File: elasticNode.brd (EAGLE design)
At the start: 82.2 x 52.5 mm, 106 parts, among them J1 ISP_CONN_6PIN, J2 FEMALE_HEADER_2X2, J3 FEMALE_HEADER_2X1, J4 FEMALE_HEADER_2X1, J5 FEMALE_HEADER_5X2, J6 FEMALE_HEADER_5X2, J7 JTAG_CONN_6PINTHT, J8 USB_CONNSMT, J9 USB_CONNSMT, U1 ATMEGA64AQFN, U10 LTC3419DFN, U11 ATMEGA32U4, U2 SST26VF032B, U3 MRF24J40MA, U4 SPARTAN6-LX9, U5 SST26VF032B, U6 PAC1720, U7 PAC1720, U8 PAC1720, U9 FT232RSSOP28, X1 12MHz, X2 50MHz, X3 32MHz

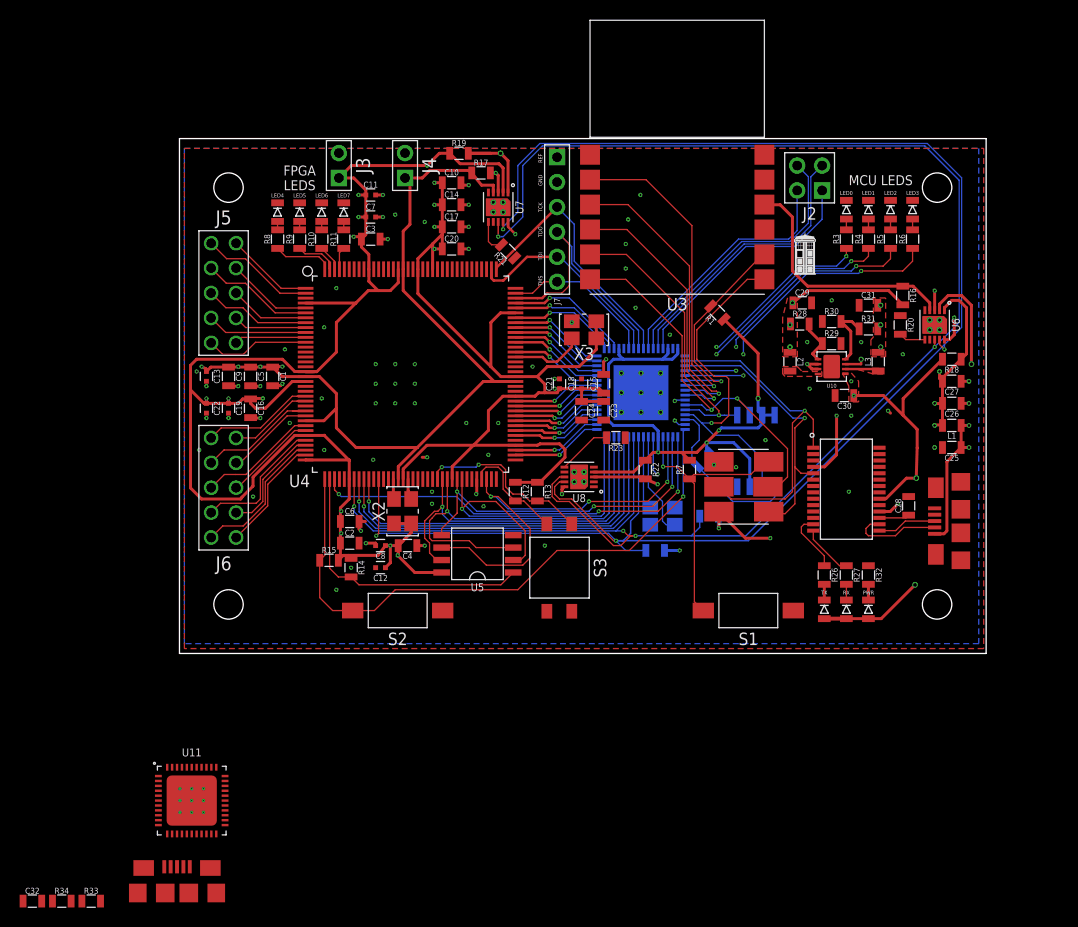
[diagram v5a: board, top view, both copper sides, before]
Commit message: first part of new layout
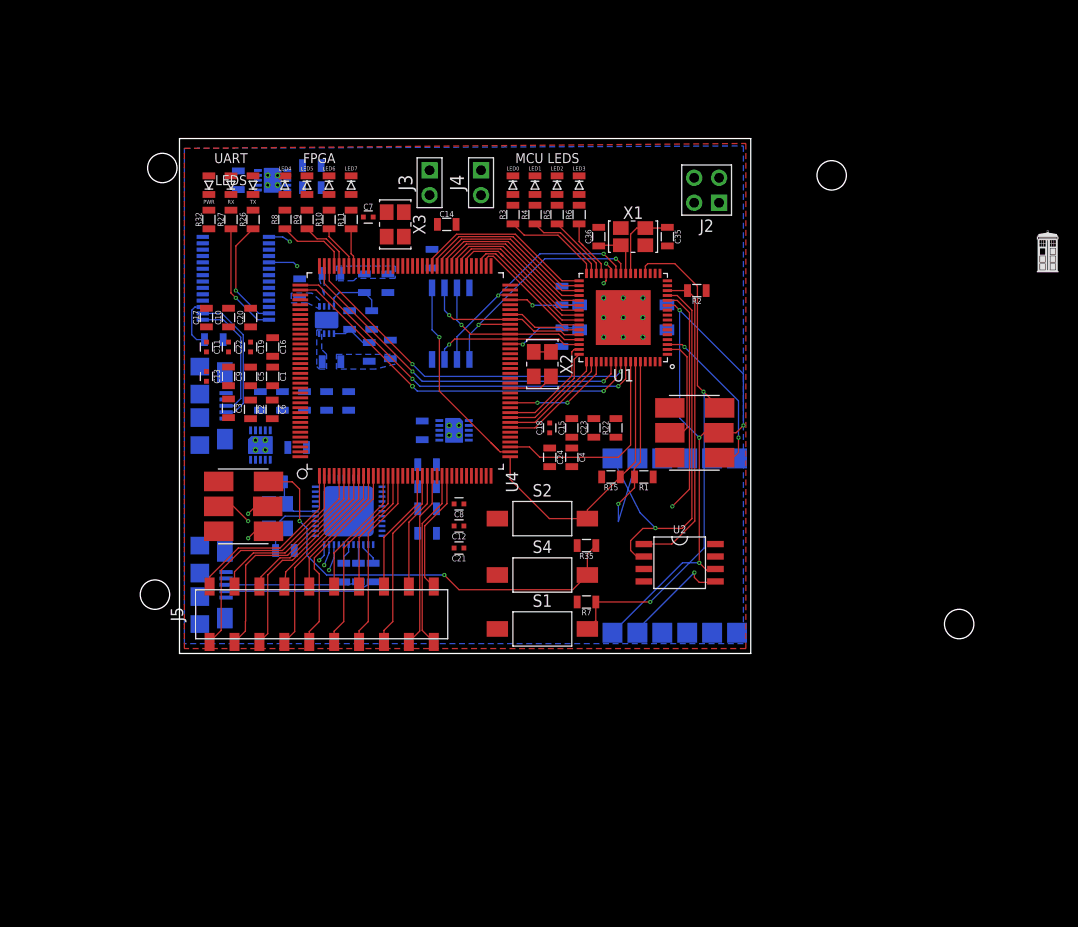
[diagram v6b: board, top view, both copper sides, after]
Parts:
- removed J6: FEMALE_HEADER_5X2, connectors:5X2_HEADER
- removed J7: JTAG_CONN_6PINTHT, connectors:6X1_HEADER
- added C33, C34: (no value), passive:0805
- added C35, C36: 20p, passive:0805
- added J10: ISP_CONN_6PIN, connectors:3X2_HEADER_SMT
- added R35: 15k, passive:0805
- added R36: .8, passive:0805
- added S4: SPST_BUTTON2PIN_SMT, connectors:SPST_2PIN_SMT
- added X4: 12MHz, passive:3.2X2.5_OSC
- J5: value FEMALE_HEADER_5X2 -> FEMALE_HEADER_10X2; device connectors:5X2_HEADER -> connectors:10X2_HEADER_SMT
- moved PWR 80.0 mm to (3.00, 47.8), turned to 270 degrees
- moved R32 76.4 mm to (3.00, 44.2), turned to 90 degrees
- moved RX 76.2 mm to (5.25, 47.8), turned to 270 degrees
- moved J8 73.2 mm to (4.75, 25.2), flipped to the bottom
- moved C28 72.8 mm to (3.50, 32.0), flipped to the bottom, turned to 180 degrees
- moved TX 72.6 mm to (7.50, 47.8), turned to 270 degrees
- moved R27 72.5 mm to (5.25, 44.2), turned to 90 degrees
- moved C25 70.7 mm to (8.25, 25.8), flipped to the bottom, turned to 90 degrees
- moved U6 69.8 mm to (8.25, 21.2), flipped to the bottom
- moved R26 68.6 mm to (7.50, 44.2), turned to 90 degrees
- moved L1 68.3 mm to (10.5, 25.8), flipped to the bottom, turned to 90 degrees
- moved C26 66.0 mm to (12.8, 25.8), flipped to the bottom, turned to 90 degrees
- moved U9 65.9 mm to (5.75, 38.2), flipped to the bottom, turned to 0 degrees
- moved C27 63.8 mm to (15.0, 25.8), flipped to the bottom, turned to 90 degrees
- moved R20 62.8 mm to (12.0, 21.0), flipped to the bottom, turned to 0 degrees
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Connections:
- net N$43 renamed UCAP
- removed net AD0: U1.51, U4.105
- removed net AD1: U1.50, U4.104
- removed net AD2: U1.49, U4.102
- removed net AD3: U1.48, U4.101
- removed net AD4: U1.47, U4.100
- removed net AD5: U1.46, U4.99
- removed net AD6: U1.45, U4.98
- removed net AD7: U1.44, U4.97
- removed net SELECTMAP_D0/FPGA_MISO1: U1.32, U4.65, U5.2
- removed net SELECTMAP_D1/FPGA_MISO2: U1.31, U4.62, U5.3
- removed net SELECTMAP_D2/FPGA_MISO3: U1.30, U4.61, U5.7
- removed net SELECTMAP_D3: U1.29, U4.46
- removed net SELECTMAP_D4/MCU_TX1: U1.28, U4.45
- removed net SELECTMAP_D5/MCU_RX1: U1.27, U4.44
- removed net SELECTMAP_D6/SDA: R25.1, U1.26, U4.43, U6.8, U7.8, U8.8
- removed net SELECTMAP_D7/SCL: R24.1, U1.25, U4.48, U6.9, U7.9, U8.9
- new net AD0/SELECTMAP_D7: U1.51, U4.48
- new net AD1/SELECTMAP_D6: U1.50, U4.43
- new net AD2/SELECTMAP_D5/MCU_RX1: U1.49, U4.44
- new net AD3/SELECTMAP_D4/MCU_TX1: U1.48, U4.45
- new net AD4/SELECTMAP_D3: U1.47, U4.46
- new net AD5/SELECTMAP_D2/FPGA_MISO3: U1.46, U4.61, U5.7
- new net AD6/SELECTMAP_D1/FPGA_MISO2: U1.45, U4.62, U5.3
- new net AD7/SELECTMAP_D0/FPGA_MISO1: U1.44, U4.65, U5.2
- new net MCU_RX1: U1.27, U9.1
- new net MCU_TX1: U1.28, U9.5
- new net MOC_VCC: J10.2
- new net MON_MISO: J10.1, U11.11
- new net MON_MOSI: J10.4, U11.10
- new net MON_RESET: J10.5, R35.1, S4.2, U11.13
- new net MON_SCK: J10.3, U11.9
- new net MON_VCC: R16.1, R35.2, U11.14, U11.24, U11.34, U11.44, U6.4
- new net MON_XTAL1: C33.1, U11.17, X4.1
- new net MON_XTAL2: C34.1, U11.16, X4.3
- new net N$33: U1.15
- new net N$46: U4.55
- new net SCL: R24.1, U11.18, U6.9, U7.9, U8.9
- new net SDA: R25.1, U11.19, U6.8, U7.8, U8.8
- net 3V3: now also R36.1, U8.1; no longer J7.P$1
- net 5V: now also R18.1, U6.1; no longer R18.2, U6.2
- net A10: now also U4.81; no longer U4.80
- net A11: now also U4.80; no longer U4.81
- net A12: now also U4.79; no longer U4.82
- net A13: now also U4.78; no longer U4.83
- net A14: now also U4.75; no longer U4.84
- net A15: now also U4.74; no longer U4.85
- net A8: now also U4.83; no longer U4.78
- net A9: now also U4.82; no longer U4.79
- net ALE: now also U4.66; no longer U4.95
- net CCLK: now also U1.26; no longer U1.19
- net CSI_B/FPGA_MISO0: now also U1.25; no longer U1.18
- net FPGA_GPIO_0: now also J5.1; no longer J5.10
- net FPGA_GPIO_1: now also J5.20; no longer J5.1
- net FPGA_GPIO_10: now also J5.15, U4.15; no longer J6.5, U4.24
- net FPGA_GPIO_11: now also J5.6, U4.14; no longer J6.6, U4.23
- net FPGA_GPIO_12: now also J5.14, U4.17; no longer J6.4, U4.27
- net FPGA_GPIO_13: now also J5.7, U4.16; no longer J6.7, U4.26
- net FPGA_GPIO_14: now also J5.8, U4.21; no longer J6.3, U4.30
- net FPGA_GPIO_15: now also J5.13, U4.22; no longer J6.8, U4.29
- net FPGA_GPIO_16: now also J5.9, U4.23; no longer J6.2, U4.33
- net FPGA_GPIO_17: now also J5.12, U4.24; no longer J6.9, U4.32
- net FPGA_GPIO_18: now also J5.10, U4.27; no longer J6.1, U4.35
- net FPGA_GPIO_19: now also J5.11, U4.26; no longer J6.10, U4.34
- net FPGA_GPIO_2: now also J5.2; no longer J5.9
- net FPGA_GPIO_3: now also J5.19; no longer J5.2
- net FPGA_GPIO_4: now also J5.3; no longer J5.8
- net FPGA_GPIO_5: now also J5.18; no longer J5.3
- net FPGA_GPIO_6: now also J5.4; no longer J5.7
- net FPGA_GPIO_7: now also J5.17; no longer J5.4
- net FPGA_GPIO_8: now also J5.5; no longer J5.6
- net FPGA_GPIO_9: now also J5.16; no longer J5.5
- net FPGA_LED0: now also U4.105; no longer U4.144
- net FPGA_LED1: now also U4.104; no longer U4.143
- net FPGA_LED2: now also U4.102; no longer U4.142
- net FPGA_LED3: now also U4.101; no longer U4.141
- net FPGA_RESET: now also U1.59; no longer U1.16
- net FPGA_VCCAUX: now also C4.1; no longer C4.2
- net GND: now also C33.2, C34.2, C35.2, C36.2, C4.2, J10.6, S4.1; no longer C4.1, J7.P$2
- net INIT_B: now also U1.58; no longer U1.17
- net JTAG_TCK: no longer J7.P$3
- net JTAG_TDI: no longer J7.P$5
- net JTAG_TDO: no longer J7.P$4
- net JTAG_TMS: no longer J7.P$6
- net MCU_GPIO_0: now also U1.16; no longer U1.58
- net MCU_GPIO_1: now also U1.6; no longer U1.59
- net MCU_GPIO_2: now also U1.17; no longer U1.60
- net MCU_LED0: now also U1.32; no longer U1.15
- net MCU_LED1: now also U1.31
- net MCU_LED2: now also U1.30
- net MCU_LED3: now also U1.29
- net MCU_RX0/PDI: no longer U9.1
- net MCU_TX0/PDO: no longer U9.5
- net RD: now also U4.84; no longer U4.75
- net USB2_VCC: no longer U11.14, U11.24, U11.34, U11.44
- net USB_VCC: now also R18.2, U6.2; no longer R18.1, U6.1
- net WIRELESS_CS: now also U1.60; no longer U1.6
- net WIRELESS_VCC: now also R36.2, U8.2; no longer R16.1, U6.4
- net WR: now also U4.85; no longer U4.74
- net XTAL1: now also C36.1, X1.1; no longer X1.3
- net XTAL2: now also C35.1, X1.3; no longer X1.1
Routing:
- net FPGA_VCCAUX: track 278.3 -> 1.75 mm, vias 16 -> 0
- net SELECTMAP_D6/SDA: track 173.6 -> 0.00 mm, vias 5 -> 0
- net SELECTMAP_D7/SCL: track 173.1 -> 0.00 mm, vias 4 -> 0
- net 5V: track 87.8 -> 0.00 mm, vias 7 -> 0
- net FPGA_VCCINT: track 87.6 -> 0.00 mm, vias 4 -> 0
- net MCU_VCC: track 67.2 -> 0.00 mm, vias 4 -> 0
- net 1V2: track 58.3 -> 0.00 mm, vias 4 -> 0
- net 3V3: track 49.2 -> 0.00 mm, vias 13 -> 0
- net MON_RESET: track 0.00 -> 45.6 mm, vias 0 -> 2
- net SELECTMAP_D1/FPGA_MISO2: track 41.0 -> 0.00 mm, vias 1 -> 0
- net SELECTMAP_D5/MCU_RX1: track 40.0 -> 0.00 mm, vias 1 -> 0
- net SELECTMAP_D4/MCU_TX1: track 38.8 -> 0.00 mm, vias 1 -> 0
- net SELECTMAP_D0/FPGA_MISO1: track 37.7 -> 0.00 mm, vias 1 -> 0
- net SELECTMAP_D3: track 37.6 -> 0.00 mm, vias 1 -> 0
- net SELECTMAP_D2/FPGA_MISO3: track 36.9 -> 0.00 mm, vias 1 -> 0
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- added copper zone on layer 16, net 1V2
- added copper zone on layer 16, net 3V3
- added copper zone on layer 16, net 5V
- added copper zone on layer 16, net N$1
- added copper zone on layer 16, net N$8
- removed copper zone on layer 1, net 1V2
- removed copper zone on layer 1, net 3V3
- removed copper zone on layer 1, net 5V
- removed copper zone on layer 1, net N$1
- removed copper zone on layer 1, net N$8
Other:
- board size 82.2 x 52.5 mm -> 58.2 x 52.5 mm
- board text added: "UART"
- board text removed: "GND"
- board text removed: "REF"
- board text removed: "TCK"
- board text removed: "TDI"
- board text removed: "TDO"
- board text removed: "TMS"

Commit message: New layout is done
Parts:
- moved R21 42.8 mm to (48.8, 48.8), turned to 90 degrees
- moved U7 35.5 mm to (45.0, 48.8), turned to 180 degrees
- moved R17 27.9 mm to (41.2, 50.2), turned to 270 degrees
- moved R19 27.9 mm to (41.2, 47.0), turned to 270 degrees
- moved R36 25.8 mm to (50.5, 22.5), turned to 180 degrees
- moved J1 24.5 mm to (53.8, 47.0), turned to 270 degrees
- moved R24 9.52 mm to (23.0, 24.0), turned to 90 degrees
- moved R25 9.28 mm to (23.0, 21.2), turned to 90 degrees
- moved R1 8.07 mm to (46.3, 26.0), turned to 0 degrees
- moved R16 7.95 mm to (17.5, 21.0), turned to 90 degrees
- moved J2 7.25 mm to (54.0, 40.0)
- moved C7 7.20 mm to (26.0, 42.0)
- moved R7 5.75 mm to (41.5, 11.0)
- moved S1 5.75 mm to (37.0, 8.25)
- moved R35 5.50 mm to (41.5, 5.50)
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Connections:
- removed net N$33: U1.15
- net 3V3: no longer R25.2
- net GND: now also U11.45
- net MCU_GPIO_0: now also J2.1, U1.17; no longer J2.4, U1.16
- net MCU_GPIO_1: now also J2.2, U1.18; no longer J2.3, U1.6
- net MCU_GPIO_2: now also J2.3, U1.19; no longer J2.2, U1.17
- net MCU_GPIO_3: now also J2.4, U1.16; no longer J2.1, U1.61
- net MCU_LED1: no longer U1.10
- net MCU_LED2: no longer U1.4
- net MCU_LED3: no longer U1.5
- net SDA: now also R25.2; no longer R25.1
- net WIRELESS_INT: now also U1.61; no longer U1.9
- net WIRELESS_RESET: now also U1.15; no longer U1.7
- net WIRELESS_WAKE: now also U1.4; no longer U1.8
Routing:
- net FPGA_VCCAUX: track 1.75 -> 265.9 mm, vias 0 -> 16
- net 3V3: track 0.00 -> 134.6 mm, vias 0 -> 13
- net FPGA_VCCINT: track 0.00 -> 109.3 mm, vias 0 -> 5
- net SDA: track 0.00 -> 81.4 mm, vias 0 -> 3
- net MON_VCC: track 0.00 -> 76.8 mm, vias 0 -> 4
- net GND: track 0.00 -> 76.0 mm, vias 0 -> 48
- net SCL: track 0.00 -> 73.2 mm
- net MCU_VCC: track 0.00 -> 66.5 mm, vias 0 -> 6
- net 5V: track 0.00 -> 63.0 mm, vias 0 -> 6
- net WIRELESS_RESET: track 0.00 -> 39.0 mm, vias 0 -> 1
- net WIRELESS_WAKE: track 0.00 -> 32.6 mm, vias 0 -> 1
- net WIRELESS_INT: track 0.00 -> 30.4 mm, vias 0 -> 1
- net WIRELESS_VCC: track 0.00 -> 29.7 mm
- net 1V2: track 0.00 -> 28.3 mm, vias 0 -> 3
- net USB2_VCC: track 0.00 -> 26.3 mm, vias 0 -> 3
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- added copper zone on layer 3, net FPGA_VCCAUX
- added copper zone on layer 3, net MCU_VCC
- removed copper zone on layer 3, net 3V3

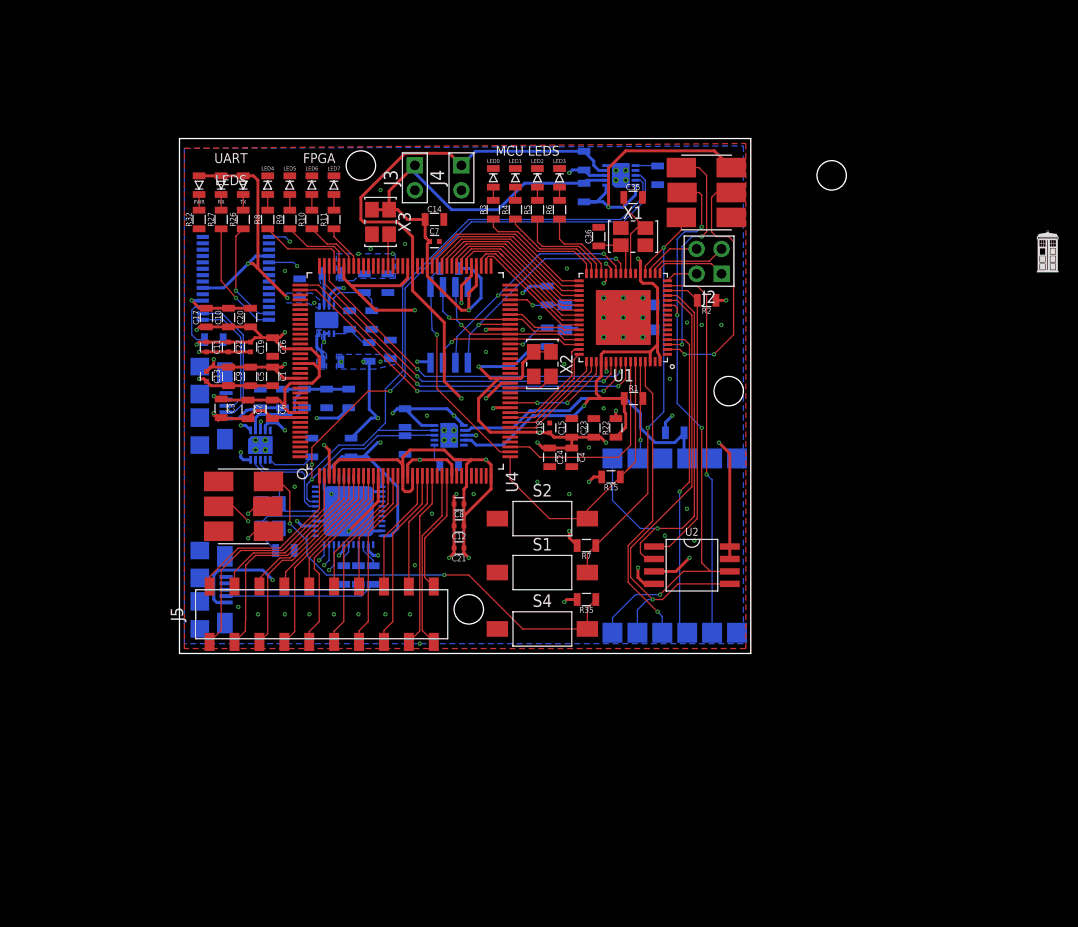
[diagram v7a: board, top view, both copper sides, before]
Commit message: elasticnode mostly finished with smaller footprint
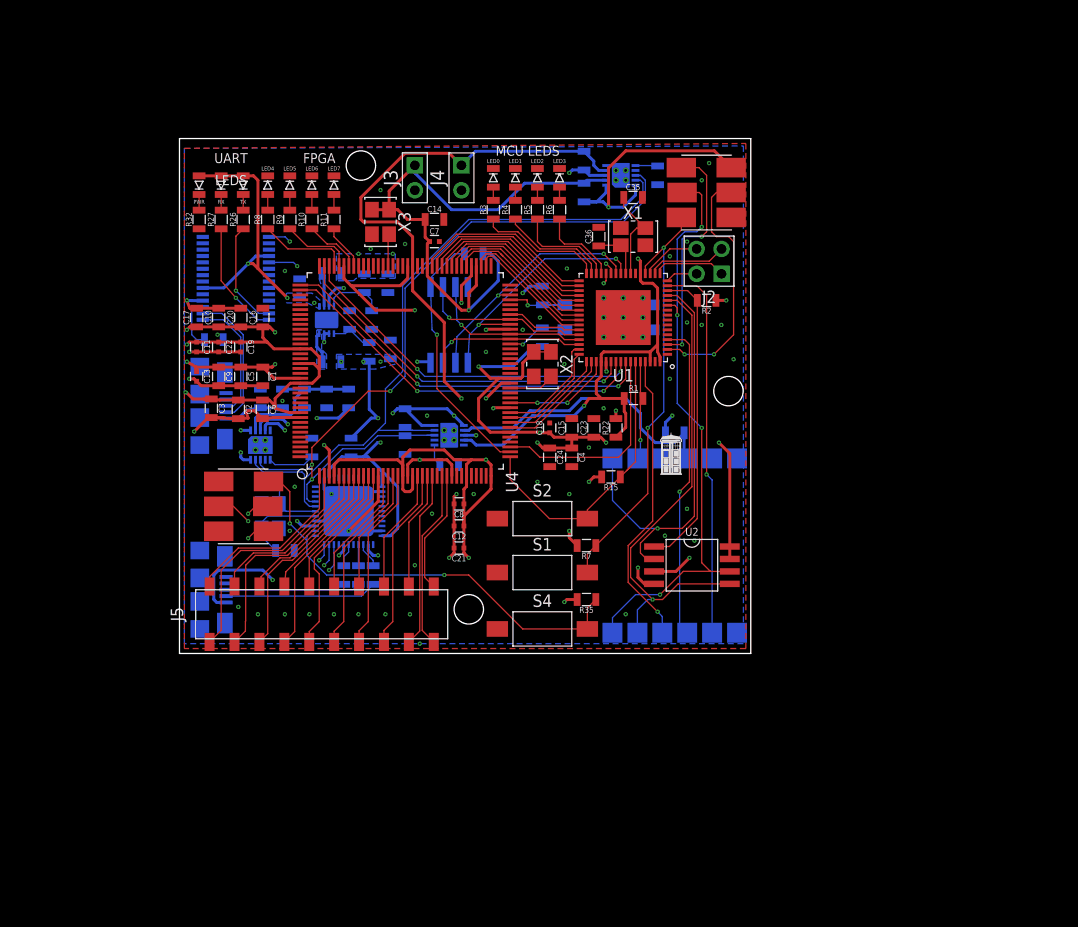
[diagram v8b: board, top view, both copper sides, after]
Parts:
- moved C16 3.16 mm to (8.50, 34.2), turned to 90 degrees
- moved R14 2.92 mm to (30.0, 40.8)
- moved C1 1.00 mm to (8.50, 28.2)
- moved C10 1.00 mm to (4.00, 34.2)
- moved C11 1.00 mm to (1.75, 31.2)
- moved C13 1.00 mm to (1.75, 28.2)
- moved C17 1.00 mm to (1.75, 34.2)
- moved C19 1.00 mm to (6.25, 31.2)
- moved C2 1.00 mm to (6.00, 24.9)
- moved C20 1.00 mm to (6.25, 34.2)
- moved C22 1.00 mm to (4.00, 31.2)
- moved C3 1.00 mm to (3.25, 25.0)
- moved C5 1.00 mm to (6.25, 28.2)
- moved C6 1.00 mm to (8.46, 24.9)
- moved C9 1.00 mm to (4.00, 28.2)
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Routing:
- net FPGA_VCCAUX: track 265.9 -> 274.4 mm
- net 3V3: track 134.6 -> 139.9 mm
- net CSO_B: track 23.0 -> 26.1 mm
- net MODE1: track 8.92 -> 6.39 mm
- net GND: track 76.0 -> 78.2 mm, vias 48 -> 56
- net FPGA_VCCINT: track 109.3 -> 111.3 mm
- net 5V: track 63.0 -> 63.7 mm
- net MODE0: track 11.7 -> 12.3 mm
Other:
- board text removed: "/Users/alwynster/git/summerProjectHardware/tardis.bmp"
